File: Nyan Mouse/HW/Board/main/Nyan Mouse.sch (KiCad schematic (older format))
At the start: 11 parts, among them M101 BATTBALANCE-2S, P101 Controller Connector, P102 CONN_4, P103 CONN_2, P104 CONN_2, U101 DRV8837, U102 DRV8837

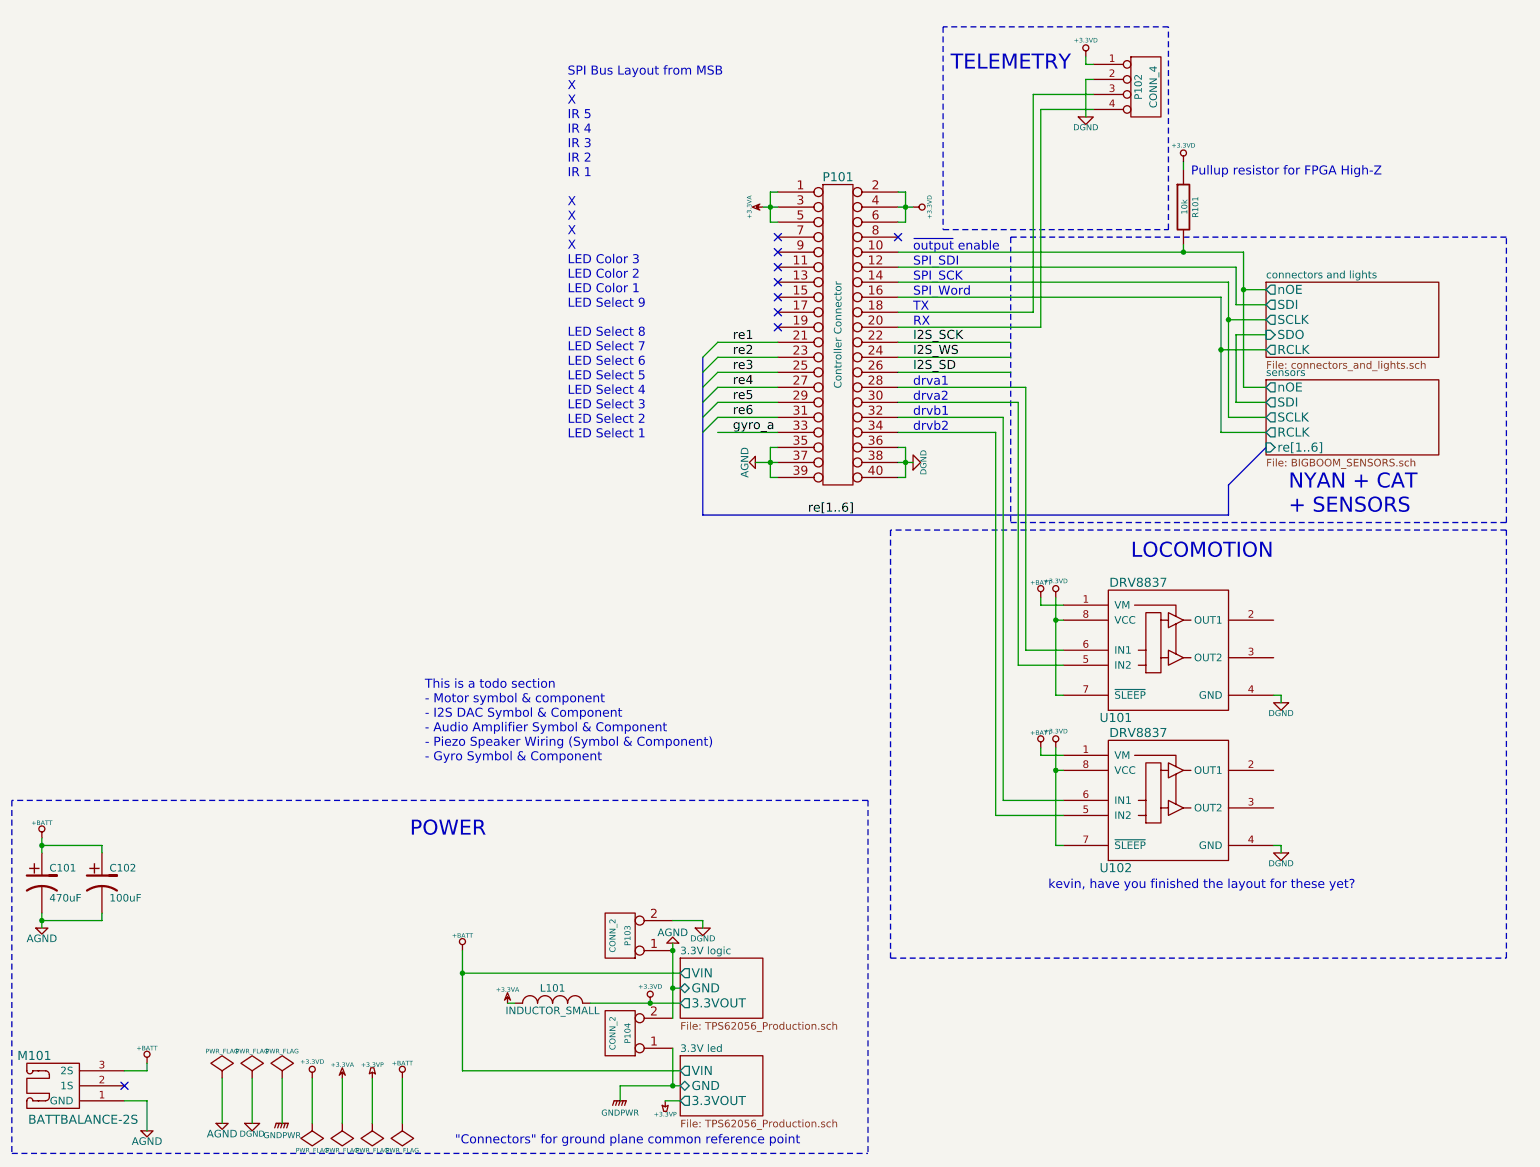
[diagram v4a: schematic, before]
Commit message: Added ESD prevention documentation.
Added ByteBlaster documentation.

Modified FPGA banks.
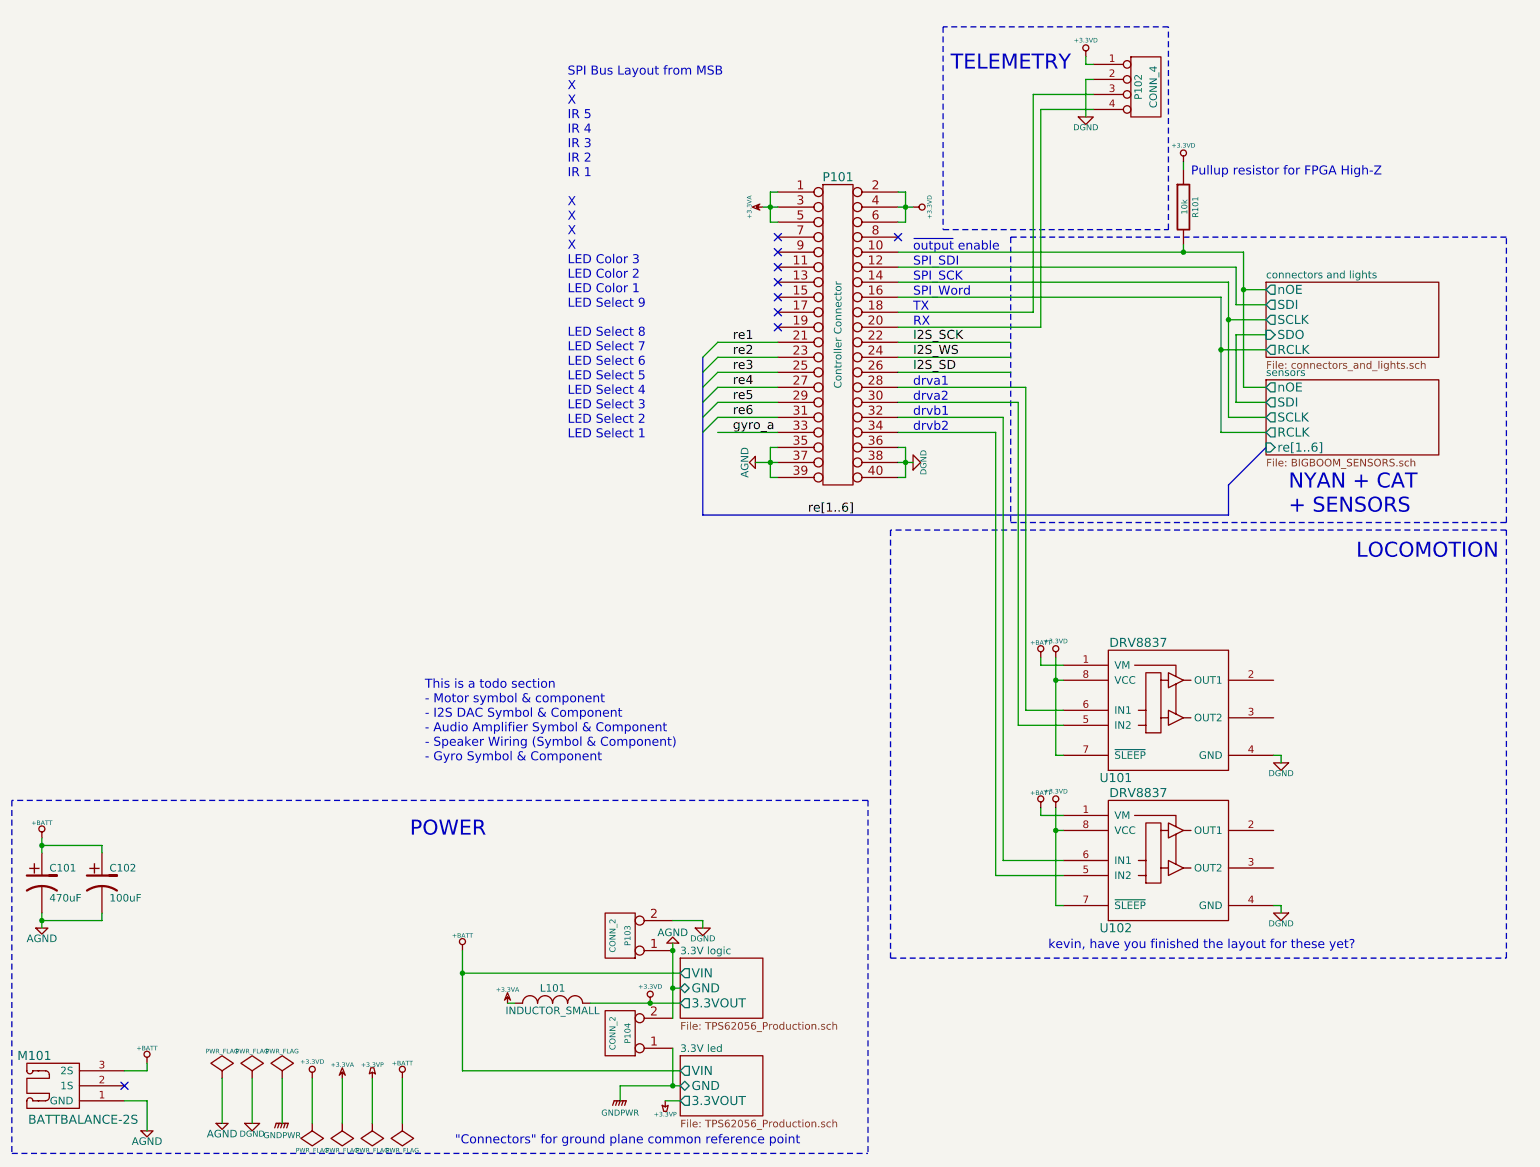
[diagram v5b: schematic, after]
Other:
- note added: "This is a todo section\n- Motor symbol & component\n- I2S DAC Symbol & Component\n- Audio Amplifier Symbol & Component\n- Speaker Wiring (Symbol & Component)\n- Gyro Symbol & Component"
- note removed: "This is a todo section\n- Motor symbol & component\n- I2S DAC Symbol & Component\n- Audio Amplifier Symbol & Component\n- Piezo Speaker Wiring (Symbol & Component)\n- Gyro Symbol & Component"
- moved on the sheet: U101, U102
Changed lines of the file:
@@
 LIBS:contrib
 LIBS:valves
+LIBS:3v3custom
+LIBS:adc128s052
+LIBS:altera_ep4ce15e22c
+LIBS:drv8837
+LIBS:JST-XH-BattBalance
+LIBS:lp3987
+LIBS:mic94345-4ycs
+LIBS:s25fl064p
+LIBS:SparkFun
+LIBS:stm32f103rx
+LIBS:tps6205x
 LIBS:Nyan Mouse-cache
 EELAYER 24 0
@@
 L DRV8837 U101
 U 1 1 5358B7EF
-P 7800 4250
-F 0 "U101" H 7850 3400 60  0000 C CNN
-F 1 "DRV8837" H 8000 4300 60  0000 C CNN
-F 2 "" H 7800 4350 60  0000 C CNN
-F 3 "" H 7800 4350 60  0000 C CNN
-	1    7800 4250
-	1    0    0    -1
-$EndComp
-Wire Wire Line
-	7450 4950 7500 4950
-Wire Wire Line
-	7450 4300 7450 4950
-Wire Wire Line
-	7450 4450 7500 4450
+P 7800 4650
+F 0 "U101" H 7850 3800 60  0000 C CNN
+F 1 "DRV8837" H 8000 4700 60  0000 C CNN
+F 2 "" H 7800 4750 60  0000 C CNN
+F 3 "" H 7800 4750 60  0000 C CNN
+	1    7800 4650
+	1    0    0    -1
+$EndComp
+Wire Wire Line
+	7450 5350 7500 5350
+Wire Wire Line
+	7450 4700 7450 5350
+Wire Wire Line
+	7450 4850 7500 4850
 $Comp
 L +BATT #PWR125
 U 1 1 5358BF77
-P 7350 4300
-F 0 "#PWR125" H 7350 4250 20  0001 C CNN
-F 1 "+BATT" H 7350 4400 30  0000 C CNN
-F 2 "" H 7350 4300 60  0000 C CNN
-F 3 "" H 7350 4300 60  0000 C CNN
-	1    7350 4300
+P 7350 4700
+F 0 "#PWR125" H 7350 4650 20  0001 C CNN
+F 1 "+BATT" H 7350 4800 30  0000 C CNN
+F 2 "" H 7350 4700 60  0000 C CNN
+F 3 "" H 7350 4700 60  0000 C CNN
+	1    7350 4700
 	-1   0    0    -1
 $EndComp
@@
 L +3.3VD #PWR127
 U 1 1 5358BF8B
-P 7450 4300
-F 0 "#PWR127" H 7450 4260 30  0001 C CNN
-F 1 "+3.3VD" H 7450 4410 30  0000 C CNN
-F 2 "" H 7450 4300 60  0000 C CNN
-F 3 "" H 7450 4300 60  0000 C CNN
-	1    7450 4300
+P 7450 4700
+F 0 "#PWR127" H 7450 4660 30  0001 C CNN
+F 1 "+3.3VD" H 7450 4810 30  0000 C CNN
+F 2 "" H 7450 4700 60  0000 C CNN
+F 3 "" H 7450 4700 60  0000 C CNN
+	1    7450 4700
 	-1   0    0    -1
 $EndComp
-Connection ~ 7450 4450
-Wire Wire Line
-	7500 4350 7350 4350
-Wire Wire Line
-	7350 4350 7350 4300
+Connection ~ 7450 4850
+Wire Wire Line
+	7500 4750 7350 4750
+Wire Wire Line
+	7350 4750 7350 4700
 $Comp
 L DGND #PWR130
 U 1 1 5358C3F5
-P 8950 5000
-F 0 "#PWR130" H 8950 5000 40  0001 C CNN
-F 1 "DGND" H 8950 4930 40  0000 C CNN
-F 2 "" H 8950 5000 60  0000 C CNN
-F 3 "" H 8950 5000 60  0000 C CNN
-	1    8950 5000
+P 8950 5400
+F 0 "#PWR130" H 8950 5400 40  0001 C CNN
+F 1 "DGND" H 8950 5330 40  0000 C CNN
+F 2 "" H 8950 5400 60  0000 C CNN
+F 3 "" H 8950 5400 60  0000 C CNN
+	1    8950 5400
 	-1   0    0    -1
 $EndComp
 Wire Wire Line
-	8900 4950 8950 4950
-Wire Wire Line
-	8950 4950 8950 5000
+	8900 5350 8950 5350
+Wire Wire Line
+	8950 5350 8950 5400
 $Comp
 L DRV8837 U102
 U 1 1 5358C8B9
-P 7800 5250
-F 0 "U102" H 7850 4400 60  0000 C CNN
-F 1 "DRV8837" H 8000 5300 60  0000 C CNN
-F 2 "" H 7800 5350 60  0000 C CNN
-F 3 "" H 7800 5350 60  0000 C CNN
-	1    7800 5250
-	1    0    0    -1
-$EndComp
-Wire Wire Line
-	7450 5950 7500 5950
-Wire Wire Line
-	7450 5300 7450 5950
-Wire Wire Line
-	7450 5450 7500 5450
+P 7800 5650
+F 0 "U102" H 7850 4800 60  0000 C CNN
+F 1 "DRV8837" H 8000 5700 60  0000 C CNN
+F 2 "" H 7800 5750 60  0000 C CNN
+F 3 "" H 7800 5750 60  0000 C CNN
+	1    7800 5650
+	1    0    0    -1
+$EndComp
+Wire Wire Line
+	7450 6350 7500 6350
+Wire Wire Line
+	7450 5700 7450 6350
+Wire Wire Line
+	7450 5850 7500 5850
 $Comp
 L +BATT #PWR126
 U 1 1 5358C8C2
-P 7350 5300
-F 0 "#PWR126" H 7350 5250 20  0001 C CNN
-F 1 "+BATT" H 7350 5400 30  0000 C CNN
-F 2 "" H 7350 5300 60  0000 C CNN
-F 3 "" H 7350 5300 60  0000 C CNN
-	1    7350 5300
+P 7350 5700
+F 0 "#PWR126" H 7350 5650 20  0001 C CNN
+F 1 "+BATT" H 7350 5800 30  0000 C CNN
+F 2 "" H 7350 5700 60  0000 C CNN
+F 3 "" H 7350 5700 60  0000 C CNN
+	1    7350 5700
 	-1   0    0    -1
 $EndComp
@@
 L +3.3VD #PWR128
 U 1 1 5358C8C8
-P 7450 5300
-F 0 "#PWR128" H 7450 5260 30  0001 C CNN
-F 1 "+3.3VD" H 7450 5410 30  0000 C CNN
-F 2 "" H 7450 5300 60  0000 C CNN
-F 3 "" H 7450 5300 60  0000 C CNN
-	1    7450 5300
+P 7450 5700
+F 0 "#PWR128" H 7450 5660 30  0001 C CNN
+F 1 "+3.3VD" H 7450 5810 30  0000 C CNN
+F 2 "" H 7450 5700 60  0000 C CNN
+F 3 "" H 7450 5700 60  0000 C CNN
+	1    7450 5700
 	-1   0    0    -1
 $EndComp
-Connection ~ 7450 5450
-Wire Wire Line
-	7500 5350 7350 5350
-Wire Wire Line
-	7350 5350 7350 5300
+Connection ~ 7450 5850
+Wire Wire Line
+	7500 5750 7350 5750
+Wire Wire Line
+	7350 5750 7350 5700
 $Comp
 L DGND #PWR131
 U 1 1 5358C8D1
-P 8950 6000
-F 0 "#PWR131" H 8950 6000 40  0001 C CNN
-F 1 "DGND" H 8950 5930 40  0000 C CNN
-F 2 "" H 8950 6000 60  0000 C CNN
-F 3 "" H 8950 6000 60  0000 C CNN
-	1    8950 6000
+P 8950 6400
+F 0 "#PWR131" H 8950 6400 40  0001 C CNN
+F 1 "DGND" H 8950 6330 40  0000 C CNN
+F 2 "" H 8950 6400 60  0000 C CNN
+F 3 "" H 8950 6400 60  0000 C CNN
+	1    8950 6400
 	-1   0    0    -1
 $EndComp
 Wire Wire Line
-	8900 5950 8950 5950
-Wire Wire Line
-	8950 5950 8950 6000
+	8900 6350 8950 6350
+Wire Wire Line
+	8950 6350 8950 6400
 Text Notes 6500 3200 0    60   ~ 0
 drvb2
@@
 	6400 2900 7250 2900
 Wire Wire Line
-	7250 2900 7250 4650
-Wire Wire Line
-	7200 4750 7200 3000
+	7250 2900 7250 5050
+Wire Wire Line
+	7200 3000 7200 5150
 Wire Wire Line
 	7200 3000 6400 3000
@@
 	6400 3100 7100 3100
 Wire Wire Line
-	7100 3100 7100 5650
-Wire Wire Line
-	7050 5750 7050 3200
+	7100 3100 7100 6050
+Wire Wire Line
+	7050 3200 7050 6150
 Wire Wire Line
 	7050 3200 6400 3200
@@
 Text Label 6500 2800 0    60   ~ 0
 I2S_SD
-Text Notes 7400 6250 0    60   ~ 0
+Text Notes 7400 6650 0    60   ~ 0
 kevin, have you finished the layout for these yet?
 NoConn ~ 6400 1900
 Text Notes 3250 5400 0    60   ~ 0
-This is a todo section\n- Motor symbol & component\n- I2S DAC Symbol & Component\n- Audio Amplifier Symbol & Component\n- Piezo Speaker Wiring (Symbol & Component)\n- Gyro Symbol & Component
+This is a todo section\n- Motor symbol & component\n- I2S DAC Symbol & Component\n- Audio Amplifier Symbol & Component\n- Speaker Wiring (Symbol & Component)\n- Gyro Symbol & Component
 Text Notes 4200 3250 0    60   ~ 0
 SPI Bus Layout from MSB\nX\nX\nIR 5\nIR 4\nIR 3\nIR 2\nIR 1\n\nX\nX\nX\nX\nLED Color 3\nLED Color 2\nLED Color 1\nLED Select 9\n\nLED Select 8\nLED Select 7\nLED Select 6\nLED Select 5\nLED Select 4\nLED Select 3\nLED Select 2\nLED Select 1
@@
 POWER
 Wire Wire Line
-	7250 4650 7500 4650
-Wire Wire Line
-	7200 4750 7500 4750
-Wire Wire Line
-	7100 5650 7500 5650
-Wire Wire Line
-	7500 5750 7050 5750
+	7250 5050 7500 5050
+Wire Wire Line
+	7200 5150 7500 5150
+Wire Wire Line
+	7100 6050 7500 6050
+Wire Wire Line
+	7050 6150 7500 6150
 Wire Notes Line
 	6350 3850 6350 6700
@@
 Wire Notes Line
 	10450 3850 6350 3850
-Text Notes 7950 4050 0    100  ~ 0
+Text Notes 9450 4050 0    100  ~ 0
 LOCOMOTION
 Wire Wire Line
